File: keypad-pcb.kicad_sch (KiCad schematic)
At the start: 21 parts, among them J1 AVR-ISP-6, SW1 SW_Push, U1 ATmega32U4-A, Y1 Crystal_GND24_Small

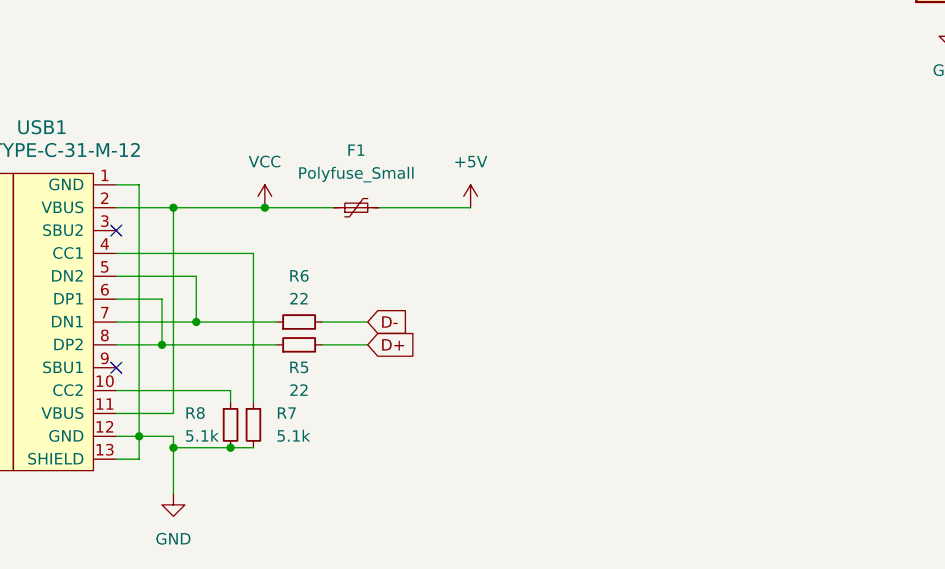
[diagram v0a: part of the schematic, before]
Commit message: esd protection
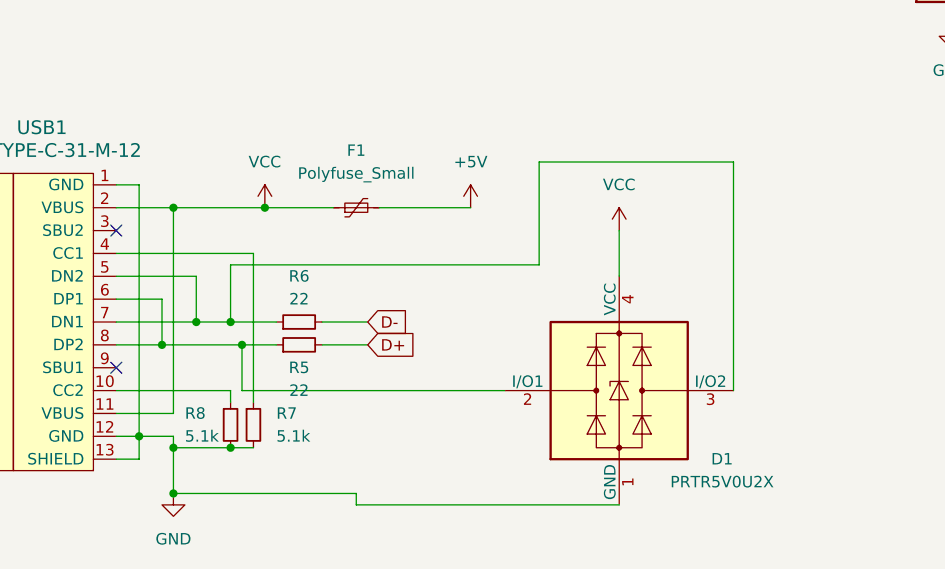
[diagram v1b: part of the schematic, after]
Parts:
- added D1: PRTR5V0U2X, Package_TO_SOT_SMD:SOT-143, symbol Power_Protection:PRTR5V0U2X
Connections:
- net GND: now also D1.1 (GND)
- net VCC: now also D1.4 (VCC)
- net at R5.1, USB1.6 (DP1), USB1.8 (DP2): now also D1.2 (I/O1)
- net at R6.1, USB1.5 (DN2), USB1.7 (DN1): now also D1.3 (I/O2)
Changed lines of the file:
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@@
   (junction (at 52.07 185.42) (diameter 0) (color 0 0 0 0)
   )
+  (junction (at 45.72 190.5) (diameter 0) (color 0 0 0 0)
+  )
+  (junction (at 53.34 173.99) (diameter 0) (color 0 0 0 0)
+  )
   (junction (at 138.43 138.43) (diameter 0) (color 0 0 0 0)
   )
@@
   )
   (junction (at 73.66 91.44) (diameter 0) (color 0 0 0 0)
+  )
+  (junction (at 52.07 171.45) (diameter 0) (color 0 0 0 0)
   )
   (junction (at 73.66 96.52) (diameter 0) (color 0 0 0 0)
@@
     (stroke (width 0) (type default))
   )
+  (wire (pts (xy 86.36 153.67) (xy 86.36 165.1))
+    (stroke (width 0) (type default))
+  )
   (wire (pts (xy 68.58 158.75) (xy 78.74 158.75))
     (stroke (width 0) (type default))
@@
     (stroke (width 0) (type default))
   )
+  (wire (pts (xy 66.04 191.77) (xy 66.04 190.5))
+    (stroke (width 0) (type default))
+  )
   (wire (pts (xy 140.97 46.99) (xy 143.51 46.99))
     (stroke (width 0) (type default))
@@
     (stroke (width 0) (type default))
   )
+  (wire (pts (xy 107.95 179.07) (xy 107.95 153.67))
+    (stroke (width 0) (type default))
+  )
   (wire (pts (xy 62.23 171.45) (xy 67.31 171.45))
     (stroke (width 0) (type default))
@@
     (stroke (width 0) (type default))
   )
+  (wire (pts (xy 95.25 161.29) (xy 95.25 166.37))
+    (stroke (width 0) (type default))
+  )
   (wire (pts (xy 48.26 166.37) (xy 48.26 171.45))
     (stroke (width 0) (type default))
@@
     (stroke (width 0) (type default))
   )
-  (wire (pts (xy 44.45 173.99) (xy 57.15 173.99))
+  (wire (pts (xy 66.04 190.5) (xy 45.72 190.5))
+    (stroke (width 0) (type default))
+  )
+  (wire (pts (xy 53.34 173.99) (xy 57.15 173.99))
+    (stroke (width 0) (type default))
+  )
+  (wire (pts (xy 44.45 173.99) (xy 53.34 173.99))
+    (stroke (width 0) (type default))
+  )
+  (wire (pts (xy 52.07 165.1) (xy 52.07 171.45))
     (stroke (width 0) (type default))
   )
@@
     (stroke (width 0) (type default))
   )
+  (wire (pts (xy 52.07 171.45) (xy 57.15 171.45))
+    (stroke (width 0) (type default))
+  )
   (wire (pts (xy 201.93 140.97) (xy 207.01 140.97))
     (stroke (width 0) (type default))
@@
     (stroke (width 0) (type default))
   )
+  (wire (pts (xy 107.95 153.67) (xy 86.36 153.67))
+    (stroke (width 0) (type default))
+  )
   (wire (pts (xy 39.37 184.15) (xy 41.91 184.15))
     (stroke (width 0) (type default))
@@
     (stroke (width 0) (type default))
   )
-  (wire (pts (xy 48.26 171.45) (xy 57.15 171.45))
+  (wire (pts (xy 48.26 171.45) (xy 52.07 171.45))
     (stroke (width 0) (type default))
   )
@@
     (stroke (width 0) (type default))
   )
+  (wire (pts (xy 95.25 191.77) (xy 66.04 191.77))
+    (stroke (width 0) (type default))
+  )
   (wire (pts (xy 64.77 96.52) (xy 73.66 96.52))
     (stroke (width 0) (type default))
@@
     (stroke (width 0) (type default))
   )
+  (wire (pts (xy 53.34 179.07) (xy 53.34 173.99))
+    (stroke (width 0) (type default))
+  )
+  (wire (pts (xy 82.55 179.07) (xy 53.34 179.07))
+    (stroke (width 0) (type default))
+  )
   (wire (pts (xy 115.57 87.63) (xy 125.73 87.63))
     (stroke (width 0) (type default))
@@
   )
   (wire (pts (xy 119.38 85.09) (xy 119.38 82.55))
+    (stroke (width 0) (type default))
+  )
+  (wire (pts (xy 86.36 165.1) (xy 52.07 165.1))
     (stroke (width 0) (type default))
   )
@@
         )
       )
+    )
+  )
+  (symbol (lib_id "power:VCC") (at 95.25 161.29 0) (unit 1)
+    (in_bom yes) (on_board yes) (dnp no) (fields_autoplaced)
+    (property "Reference" "#PWR015" (at 95.25 165.1 0)
+      (effects (font (size 1.27 1.27)) hide)
+    )
+    (property "Value" "VCC" (at 95.25 156.21 0)
+      (effects (font (size 1.27 1.27)))
+    )
+    (property "Footprint" "" (at 95.25 161.29 0)
+      (effects (font (size 1.27 1.27)) hide)
+    )
+    (property "Datasheet" "" (at 95.25 161.29 0)
+      (effects (font (size 1.27 1.27)) hide)
+    )
+    (pin "1")
+    (instances
+      (project "keypad-pcb"
+        (path "/73f1bcf6-a3cb-4955-8c73-ee07117345ce"
+          (reference "#PWR015") (unit 1)
+        )
+      )
+    )
+  )
+  (symbol (lib_id "Power_Protection:PRTR5V0U2X") (at 95.25 179.07 0) (unit 1)
+    (in_bom yes) (on_board yes) (dnp no)
+    (property "Reference" "D1" (at 106.68 186.69 0)
+      (effects (font (size 1.27 1.27)))
+    )
+    (property "Value" "PRTR5V0U2X" (at 106.68 189.23 0)
+      (effects (font (size 1.27 1.27)))
+    )
+    (property "Footprint" "Package_TO_SOT_SMD:SOT-143" (at 96.774 179.07 0)
+      (effects (font (size 1.27 1.27)) hide)
+    )
+    (property "Datasheet" "https://assets.nexperia.com/documents/data-sheet/PRTR5V0U2X.pdf" (at 96.774 179.07 0)
+      (effects (font (size 1.27 1.27)) hide)
+    )
+    (pin "1")
+    (pin "4")
+    (pin "3")
+    (pin "2")
+    (instances
+      (project "keypad-pcb"
+        (path "/73f1bcf6-a3cb-4955-8c73-ee07117345ce"
+          (reference "D1") (unit 1)
+        )
+      )

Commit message: matrix
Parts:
- added D2, D3, D4, D5, D6, D7: D, symbol Device:D
- added SW1, SW2, SW3, SW4, SW5, SW6: SW_Push, symbol Switch:SW_Push
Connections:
- new net: D7.2 (A), SW3.1
- new net: D4.2 (A), SW4.1
- new net: D6.2 (A), SW2.1
- new net: D2.2 (A), SW1.1
- new net: D3.2 (A), SW5.1
- new net: D5.2 (A), SW6.1
- new net COL0: SW1.2, SW4.2
- new net COL1: SW2.2, SW5.2
- new net COL2: SW3.2, SW6.2
- new net ROW0: D2.1 (K), D6.1 (K), D7.1 (K)
- new net ROW1: D3.1 (K), D4.1 (K), D5.1 (K)

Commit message: mcu wiring
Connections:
- net +5V: now also U1.7 (VBUS)
- net COL0: now also U1.41 (PF0)
- net COL1: now also U1.39 (PF4)
- net COL2: now also U1.37 (PF6)
- net ROW0: now also U1.28 (PB4)
- net ROW1: now also U1.30 (PB6)
- no-connect marks 2 -> 20
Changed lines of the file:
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@@
   (junction (at 35.56 39.37) (diameter 0) (color 0 0 0 0)
   )
+  (no_connect (at 156.21 85.09))
+  (no_connect (at 156.21 97.79))
+  (no_connect (at 156.21 128.27))
+  (no_connect (at 156.21 80.01))
+  (no_connect (at 156.21 102.87))
+  (no_connect (at 156.21 67.31))
   (no_connect (at 39.37 176.53))
+  (no_connect (at 156.21 72.39))
+  (no_connect (at 156.21 123.19))
+  (no_connect (at 156.21 92.71))
+  (no_connect (at 125.73 69.85))
+  (no_connect (at 156.21 110.49))
+  (no_connect (at 156.21 54.61))
+  (no_connect (at 156.21 95.25))
+  (no_connect (at 156.21 118.11))
   (no_connect (at 39.37 161.29))
+  (no_connect (at 156.21 77.47))
+  (no_connect (at 156.21 100.33))
+  (no_connect (at 156.21 87.63))
+  (no_connect (at 156.21 90.17))
   (wire (pts (xy 217.17 69.85) (xy 217.17 78.74))
     (stroke (width 0) (type default))
@@
     (stroke (width 0) (type default))
   )
+  (wire (pts (xy 121.92 74.93) (xy 125.73 74.93))
+    (stroke (width 0) (type default))
+  )
   (wire (pts (xy 101.6 76.2) (xy 114.3 76.2))
     (stroke (width 0) (type default))
@@
     (stroke (width 0) (type default))
   )
+  (wire (pts (xy 162.56 120.65) (xy 156.21 120.65))
+    (stroke (width 0) (type default))
+  )
   (wire (pts (xy 196.85 140.97) (xy 201.93 140.97))
     (stroke (width 0) (type default))
@@
     (stroke (width 0) (type default))
   )
+  (wire (pts (xy 165.1 64.77) (xy 156.21 64.77))
+    (stroke (width 0) (type default))
+  )
+  (wire (pts (xy 162.56 115.57) (xy 156.21 115.57))
+    (stroke (width 0) (type default))
+  )
   (wire (pts (xy 81.28 21.59) (xy 81.28 31.75))
     (stroke (width 0) (type default))
@@
     (stroke (width 0) (type default))
   )
+  (wire (pts (xy 165.1 69.85) (xy 156.21 69.85))
+    (stroke (width 0) (type default))
+  )
   (wire (pts (xy 229.87 86.36) (xy 242.57 86.36))
     (stroke (width 0) (type default))
@@
     (stroke (width 0) (type default))
   )
+  (wire (pts (xy 162.56 125.73) (xy 156.21 125.73))
+    (stroke (width 0) (type default))
+  )
   (wire (pts (xy 53.34 179.07) (xy 53.34 173.99))
     (stroke (width 0) (type default))
@@
     (stroke (width 0) (type default))
   )
-  (wire (pts (xy 166.37 107.95) (xy 171.45 107.95))
+  (wire (pts (xy 166.37 107.95) (xy 175.26 107.95))
     (stroke (width 0) (type default))
   )
@@
   (wire (pts (xy 115.57 92.71) (xy 115.57 99.06))
     (stroke (width 0) (type default))
+  )
+  (global_label "ROW1" (shape input) (at 165.1 69.85 0) (fields_autoplaced)
+    (effects (font (size 1.27 1.27)) (justify left))
+    (property "Intersheetrefs" "${INTERSHEET_REFS}" (at 173.3466 69.85 0)
+      (effects (font (size 1.27 1.27)) (justify left) hide)
+    )
   )
   (global_label "D-" (shape input) (at 101.6 85.09 180) (fields_autoplaced)
@@
     )
   )
+  (global_label "COL2" (shape input) (at 162.56 125.73 0) (fields_autoplaced)
+    (effects (font (size 1.27 1.27)) (justify left))
+    (property "Intersheetrefs" "${INTERSHEET_REFS}" (at 170.3833 125.73 0)
+      (effects (font (size 1.27 1.27)) (justify left) hide)
+    )
+  )
   (global_label "D+" (shape input) (at 67.31 173.99 0) (fields_autoplaced)
     (effects (font (size 1.27 1.27)) (justify left))
@@
     )
   )
+  (global_label "COL0" (shape input) (at 162.56 115.57 0) (fields_autoplaced)
+    (effects (font (size 1.27 1.27)) (justify left))
+    (property "Intersheetrefs" "${INTERSHEET_REFS}" (at 170.3833 115.57 0)
+      (effects (font (size 1.27 1.27)) (justify left) hide)
+    )
+  )
   (global_label "MOSI" (shape input) (at 240.03 119.38 0) (fields_autoplaced)
     (effects (font (size 1.27 1.27)) (justify left))
@@
     )
   )
+  (global_label "ROW0" (shape input) (at 165.1 64.77 0) (fields_autoplaced)
+    (effects (font (size 1.27 1.27)) (justify left))
+    (property "Intersheetrefs" "${INTERSHEET_REFS}" (at 173.3466 64.77 0)
+      (effects (font (size 1.27 1.27)) (justify left) hide)
+    )
+  )
   (global_label "XTAL1" (shape input) (at 217.17 57.15 180) (fields_autoplaced)
     (effects (font (size 1.27 1.27)) (justify right))
     (property "Intersheetrefs" "${INTERSHEET_REFS}" (at 208.6815 57.15 0)
       (effects (font (size 1.27 1.27)) (justify right) hide)
+    )
+  )
+  (global_label "COL1" (shape input) (at 162.56 120.65 0) (fields_autoplaced)
+    (effects (font (size 1.27 1.27)) (justify left))
+    (property "Intersheetrefs" "${INTERSHEET_REFS}" (at 170.3833 120.65 0)
+      (effects (font (size 1.27 1.27)) (justify left) hide)
+    )
+  )
+  (symbol (lib_id "power:+5V") (at 121.92 74.93 0) (unit 1)
+    (in_bom yes) (on_board yes) (dnp no) (fields_autoplaced)
+    (property "Reference" "#PWR016" (at 121.92 78.74 0)
+      (effects (font (size 1.27 1.27)) hide)
+    )
+    (property "Value" "+5V" (at 121.92 69.85 0)
+      (effects (font (size 1.27 1.27)))
+    )
+    (property "Footprint" "" (at 121.92 74.93 0)
+      (effects (font (size 1.27 1.27)) hide)
+    )
+    (property "Datasheet" "" (at 121.92 74.93 0)
+      (effects (font (size 1.27 1.27)) hide)
+    )
+    (pin "1")
+    (instances
+      (project "keypad-pcb"
+        (path "/73f1bcf6-a3cb-4955-8c73-ee07117345ce"
+          (reference "#PWR016") (unit 1)
+        )
+      )
     )
   )
@@
     )
   )
-  (symbol (lib_id "power:GND") (at 171.45 107.95 0) (unit 1)
-    (in_bom yes) (on_board yes) (dnp no) (fields_autoplaced)
-    (property "Reference" "#PWR03" (at 171.45 114.3 0)
-      (effects (font (size 1.27 1.27)) hide)
-    )
-    (property "Value" "GND" (at 171.45 113.03 0)
-      (effects (font (size 1.27 1.27)))
-    )
-    (property "Footprint" "" (at 171.45 107.95 0)
-      (effects (font (size 1.27 1.27)) hide)
-    )
-    (property "Datasheet" "" (at 171.45 107.95 0)
-      (effects (font (size 1.27 1.27)) hide)
-    )
+  (symbol (lib_id "power:GND") (at 175.26 107.95 0) (unit 1)
+    (in_bom yes) (on_board yes) (dnp no) (fields_autoplaced)
+    (property "Reference" "#PWR03" (at 175.26 114.3 0)
+      (effects (font (size 1.27 1.27)) hide)
+    )
+    (property "Value" "GND" (at 175.26 113.03 0)
+      (effects (font (size 1.27 1.27)))
+    )
+    (property "Footprint" "" (at 175.26 107.95 0)
+      (effects (font (size 1.27 1.27)) hide)
+    )
+    (property "Datasheet" "" (at 175.26 107.95 0)
+      (effects (font (size 1.27 1.27)) hide)
+    )
